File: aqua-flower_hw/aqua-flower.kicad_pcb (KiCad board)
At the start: 2 copper layers, 84 x 45 mm, 40 parts, among them Q1 NPN, Q2 IRLML6302, Q5 IRLML6302, SW1 BUTTON, SW2 BUTTON, SW3 BUTTON, SW4 BUTTON, SW5 BUTTON, SW6 BUTTON

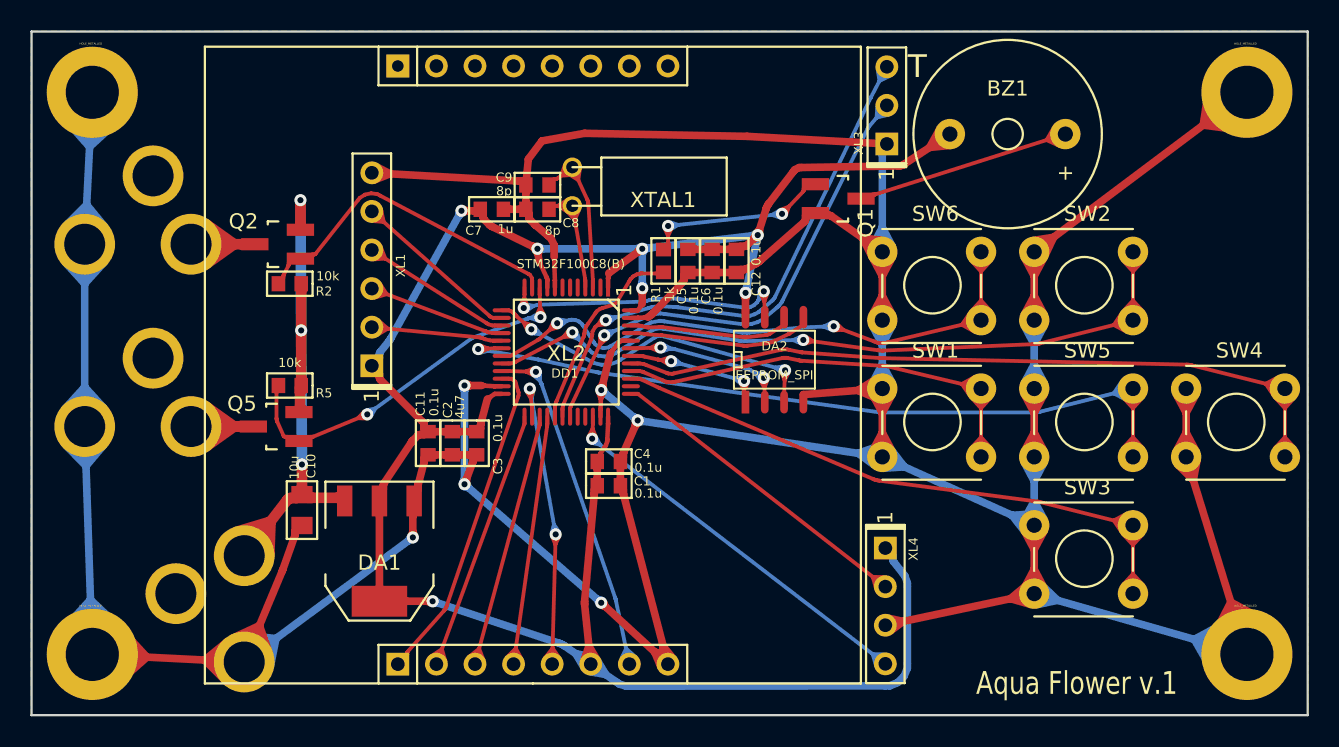
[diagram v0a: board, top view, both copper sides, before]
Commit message: Update PCB try to reach no error in rezonit
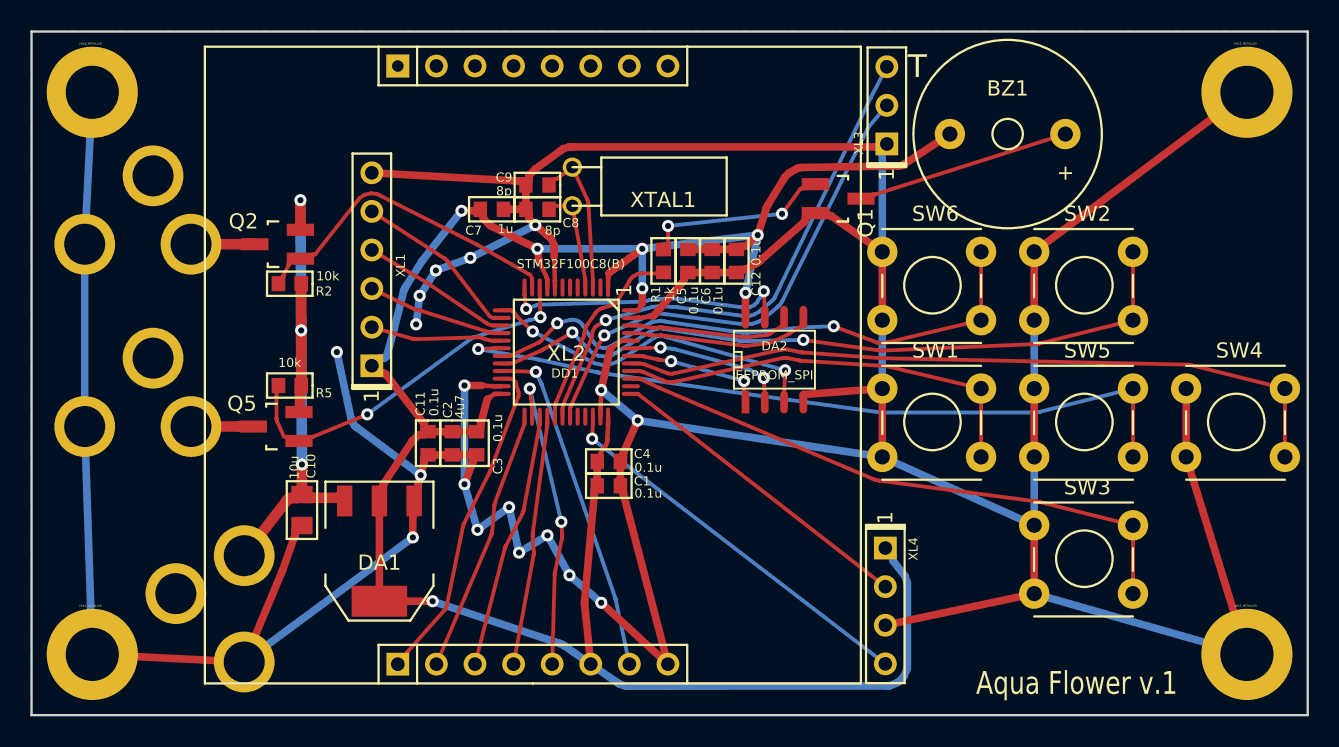
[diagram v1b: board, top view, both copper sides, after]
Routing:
- net GND: track 494.0 -> 363.4 mm, vias 6 -> 18
- net +3.3V: track 179.8 -> 158.4 mm
- net /BTN_UP: track 58.5 -> 48.0 mm
- net /BTN_CANCEL: track 49.1 -> 38.6 mm
- net /BTN_OK: track 57.8 -> 49.7 mm
- net /LCD_CLK: track 26.6 -> 20.3 mm
- net /BTN_DOWN: track 45.0 -> 39.2 mm
- net /BTN_RIGHT: track 53.8 -> 48.1 mm
- net /BTN_LEFT: track 33.8 -> 28.1 mm
- net /EE_HOLD: track 24.3 -> 19.4 mm
- net /CH1_POWER: track 29.4 -> 24.5 mm
- net /EE_MISO: track 15.5 -> 10.7 mm
- net Net-(Q1-Pad1): track 17.1 -> 12.3 mm
- net /EE_CS: track 13.8 -> 9.06 mm
- net /EE_WP: track 27.4 -> 22.7 mm
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
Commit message: follow up
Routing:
- net GND: track 363.4 -> 368.0 mm, vias 18 -> 21
- net /BTN_CANCEL: track 38.6 -> 37.7 mm
- net /EE_HOLD: track 19.4 -> 20.2 mm
- net /BTN_UP: track 48.0 -> 47.2 mm
